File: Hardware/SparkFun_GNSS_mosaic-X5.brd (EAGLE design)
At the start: 63.5 x 50.8 mm, 169 parts, among them J3 MICROSD, J5 USB Female Type C Connector, U1 MOSAIC-X5X5, U2 SN74AHC1G125DBVR, U5 AP2112K-3.3V

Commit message: Route board.
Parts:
- removed U$1: (no value), output:MOSAIC_0
- removed U$139: (no value), output:MOSAIC0
- added R1: 10k, SparkFun-Resistors:0603
- added U$19: (no value), output:MOSAIC#X50
- added U$20: (no value), output:MOSAIC#X5_0
- moved U$87 2.54 mm to (15.2, 4.19)
- moved U$89 2.54 mm to (12.7, 4.06)
- moved U$93 2.54 mm to (15.2, 4.06)
- moved U$95 2.54 mm to (12.7, 3.94)
- moved C5 2.54 mm to (17.8, 27.9), turned to 0 degrees
- moved U$110 2.54 mm to (20.3, 46.7)
- moved U$113 2.54 mm to (17.8, 46.9)
- moved U$114 2.54 mm to (20.3, 46.6)
- moved U$117 2.54 mm to (17.8, 46.7)
- moved U$123 2.54 mm to (22.9, 47.0)
- moved U$124 2.54 mm to (25.4, 46.4)
- moved U$130 2.54 mm to (22.9, 47.0)
- moved U$131 2.54 mm to (25.4, 46.2)
- moved R17 1.27 mm to (10.2, 14.0)
- moved R16 1.27 mm to (10.2, 6.35)
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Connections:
- net PPS_18V renamed PPS_1V8
- new net N$5: J3.2, R1.1
- net 3.3V: now also R1.2
- net D+: now also D1.6; no longer D1.4
- net D-: now also D1.4; no longer D1.6
- net VIN: now also J7.3; no longer J7.4
- net V_USB: now also J7.4; no longer J7.3
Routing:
- net 3.3V: track 0.00 -> 155.8 mm, vias 0 -> 4
- net V_USB: track 0.00 -> 89.0 mm, vias 0 -> 4
- net LOG_BTN: track 0.00 -> 88.9 mm, vias 0 -> 4
- net SD_CMD: track 0.00 -> 70.2 mm, vias 0 -> 2
- net SD_CLK: track 0.00 -> 67.8 mm, vias 0 -> 2
- net SD_DATA: track 0.00 -> 67.2 mm, vias 0 -> 2
- net V_BAT: track 0.00 -> 66.3 mm, vias 0 -> 2
- net 5V: track 0.00 -> 66.0 mm, vias 0 -> 2
- net PPS_3V3: track 0.00 -> 59.0 mm, vias 0 -> 2
- net !RESET!: track 0.00 -> 51.6 mm, vias 0 -> 4
- net LOG_LED: track 0.00 -> 50.3 mm, vias 0 -> 3
- net COM3_CTS: track 0.00 -> 48.1 mm, vias 0 -> 2
- net VIN: track 0.00 -> 47.6 mm, vias 0 -> 1
- net COM3_TX: track 0.00 -> 47.1 mm, vias 0 -> 3
- net COM3_RX: track 0.00 -> 44.8 mm, vias 0 -> 2
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
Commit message: Add jumper to ant voltage. Add production panel.
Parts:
- removed C1: 0.1uF, SparkFun-Capacitors:0603
- removed J10: (no value), SparkFun-Connectors:1X06_NO_SILK
- removed L1: 39nH, SparkFun-Coils:0603
- removed U$78: (no value), output:GP1
- added ANT_V: (no value), SparkFun-Jumpers:SMT-JUMPER_3_1-NC_TRACE_SILK
- added D2: WHITE, SparkFun-LED:LED-0603
- added GP2: JUMPER-SMT_2_NC_TRACE_SILK, SparkFun-Jumpers:SMT-JUMPER_2_NC_TRACE_SILK
- added J6: (no value), SparkFun-Connectors:1X07_NO_SILK
- added Q9: 20V/0.2A/8MHz/1.2Ω/1Vth, SparkFun-DiscreteSemi:SOT-416FL
- added R46, R47: 2.2k, SparkFun-Resistors:0603
- added R6, R7: 169K, SparkFun-Resistors:0603@1
- added R9: 1k, SparkFun-Resistors:0603@1
- added U$1: (no value), output:V0
- added U$22: (no value), output:G1
- added U$23: (no value), output:3V30
- added U$24: (no value), output:5V0
- added U$26: (no value), output:#ANT_V#0
- added U$27: (no value), output:#RTK_LED#0
- added U$28: (no value), output:RTK0
- added U$29: (no value), output:PVT0
- R1, R10, R16, R17, R2, R3, R5, R8: device SparkFun-Resistors:0603 -> SparkFun-Resistors:0603@1
- R11, R4: value 1k -> 2.2k
- R12: value 1k -> 330; device SparkFun-Resistors:0603 -> SparkFun-Resistors:0603@1
- U$17: device output:#1 -> output:#_RTK#0
- U$7: device output:#0 -> output:#RTK#0
- U1: device Septentrio_Mosaic:MOSAIC-X5 -> Septentriom_mosaic-X5:MOSAIC_LGA
- moved U$7 47.0 mm to (45.7, 3.94), flipped to the top, turned to 90 degrees
- moved U$17 43.7 mm to (45.7, 4.06), turned to 270 degrees
- moved U$3 3.81 mm to (31.4, 21.6)
- moved U$4 3.81 mm to (31.2, 25.4)
- moved J1 2.54 mm to (25.4, 1.27)
- moved U$101 2.54 mm to (30.5, 3.94)
- moved U$102 2.54 mm to (25.4, 3.56)
- moved U$105 2.54 mm to (30.5, 3.68)
- moved U$106 2.54 mm to (25.4, 3.17)
- moved U$109 2.54 mm to (18.9, 7.62)
- moved J9 2.54 mm to (15.2, 1.27)
- moved U$87 2.54 mm to (12.7, 4.19)
- moved U$91 2.54 mm to (15.2, 3.56)
- moved U$93 2.54 mm to (12.7, 4.06)
- moved U$97 2.54 mm to (15.2, 3.17)
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- renumbered GP to GP1
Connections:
- net GP_LED renamed PVT_LED
- removed net ANT_VCC: C1.1, L1.2
- new net ANT_V: ANT_V.2, C3.1, FB1.1
- new net ICM-20948-LV_#_1.8V: Q9.1, R46.2
- new net N$6: R6.1, U1.AC6
- new net N$7: R7.1, U1.AC7
- new net N$8: D2.A, R9.1
- new net N$9: GP2.1, R9.2
- new net PPS_3: Q9.3, R47.1, U2.2
- new net RTK_LED: GP2.2, J6.3, U1.M3
- net 3.3V: now also ANT_V.1, R47.2
- net 5V: now also ANT_V.3; no longer C3.1, FB1.1
- net EVENTA: now also J6.6, R6.2; no longer J10.5, U1.AC6
- net EVENTB: now also J6.7, R7.2; no longer J10.6, U1.AC7
- net GND: now also D2.C, U1.V23; no longer C1.2
- net GP1: now also J6.1; no longer J10.1
- net GP2: now also J6.2; no longer J10.2
- net GPS_ANT1: no longer L1.1
- net LOG_BTN: now also J6.4; no longer J10.3
- net PPS_1V8: now also Q9.2, R46.1; no longer U2.2
- net PPS_3V3: now also J6.5; no longer J10.4
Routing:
- net RTK_LED: track 0.00 -> 51.6 mm, vias 0 -> 2
- net ANT_V: track 0.00 -> 17.1 mm, vias 0 -> 1
- net 5V: track 66.0 -> 49.0 mm, vias 2 -> 3
- net PPS_3: track 0.00 -> 15.6 mm
- net V_BAT: track 66.3 -> 52.3 mm, vias 2 -> 3
- net 3.3V: track 155.8 -> 165.9 mm, vias 4 -> 6
- net PPS_1V8: track 6.96 -> 15.9 mm
- net N$7: track 0.00 -> 4.91 mm
- net N$6: track 0.00 -> 4.65 mm
- net EVENTA: track 17.6 -> 22.1 mm
- net N$9: track 0.00 -> 4.06 mm, vias 0 -> 1
- net EVENTB: track 19.9 -> 23.4 mm
- net COM2_TX: track 10.7 -> 13.2 mm
- net ANT_VCC: track 2.32 -> 0.00 mm
- net GP1: track 31.0 -> 33.1 mm, vias 2 -> 1
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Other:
- board text added: "15"
- board text added: "2"
- board text added: "Material: TG155"

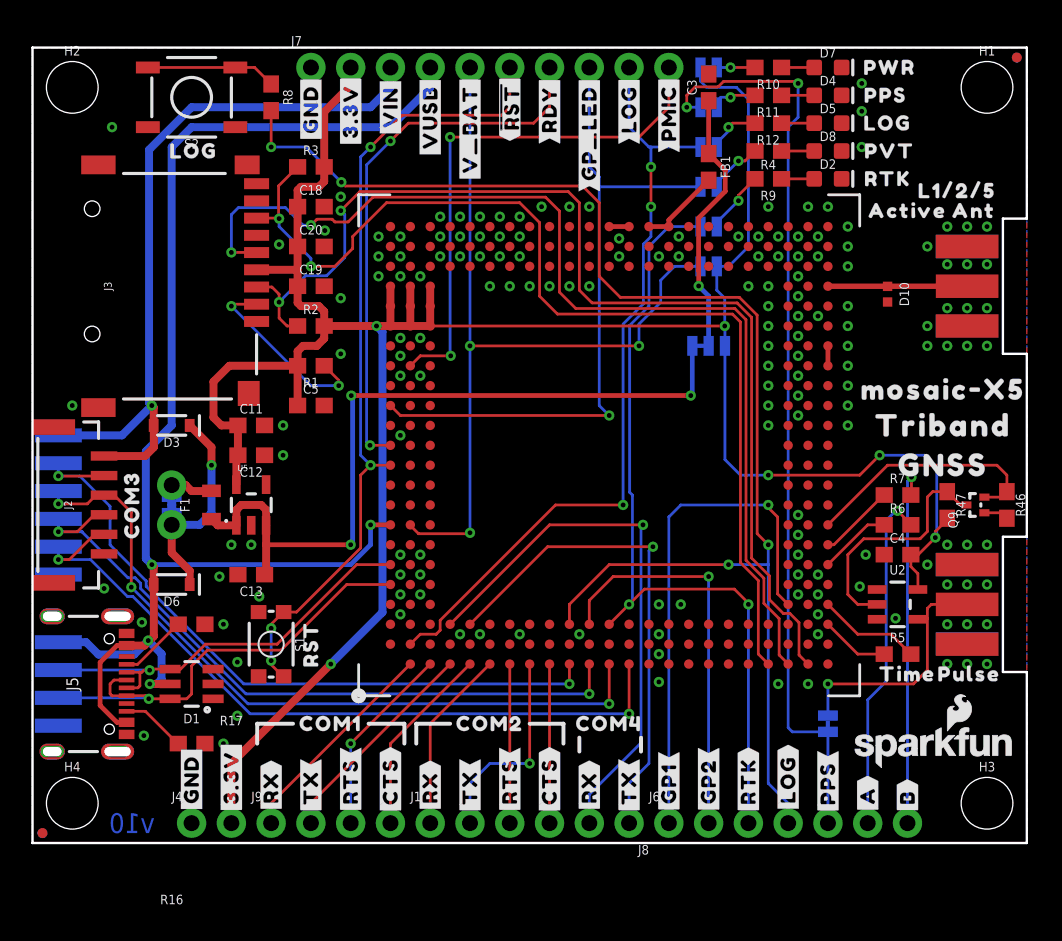
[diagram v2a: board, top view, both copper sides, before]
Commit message: Fixed tCream on mosaic pin 1.
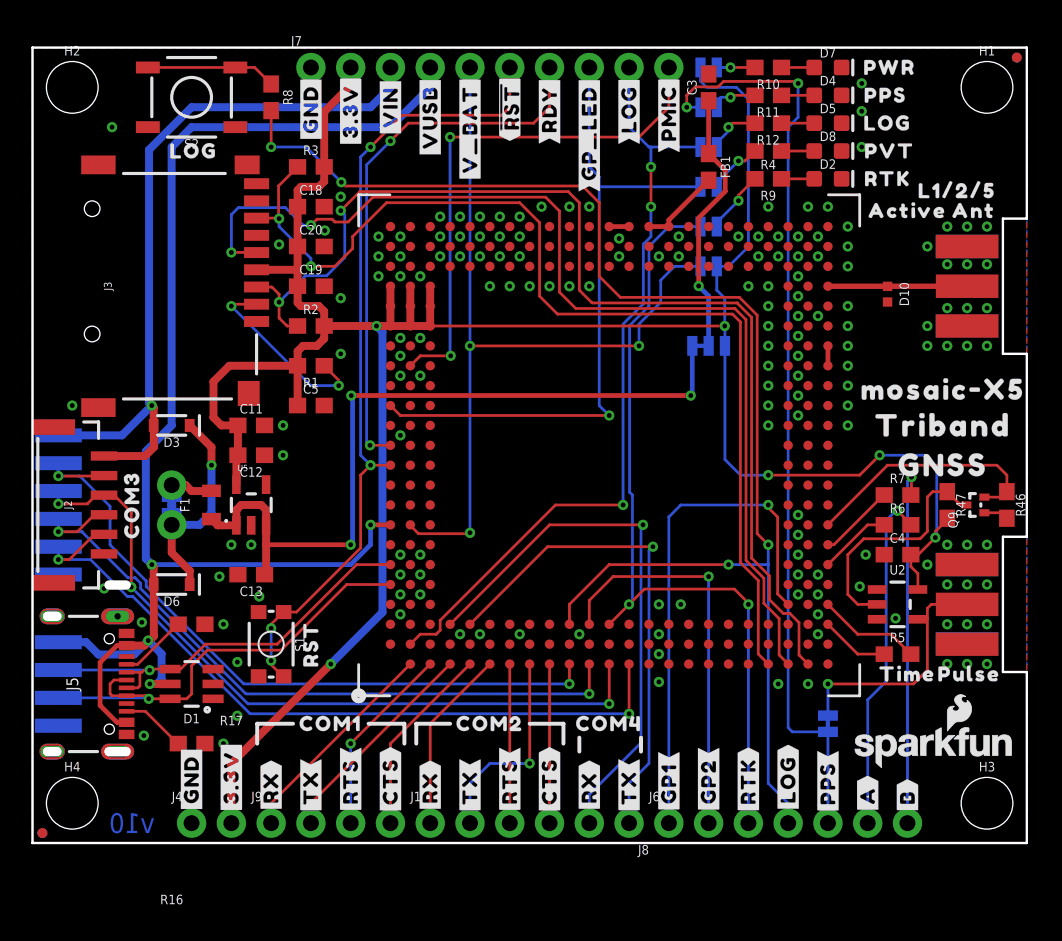
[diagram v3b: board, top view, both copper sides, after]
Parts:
- added U$30: (no value), output:MADE_IN_AMERICA0
- R1, R10, R12, R16, R17, R2, R3, R5, R6, R7, R8, R9: device SparkFun-Resistors:0603@1 -> SparkFun-Resistors:0603
- U1: device Septentriom_mosaic-X5:MOSAIC_LGA -> Septentrio_mosaic-X5:MOSAIC_LGA
- U5: value AP2112K-3.3V -> 3.3V
- moved LOGO1 3.81 mm to (31.8, 36.4)

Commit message: Add ESD and USB choke.
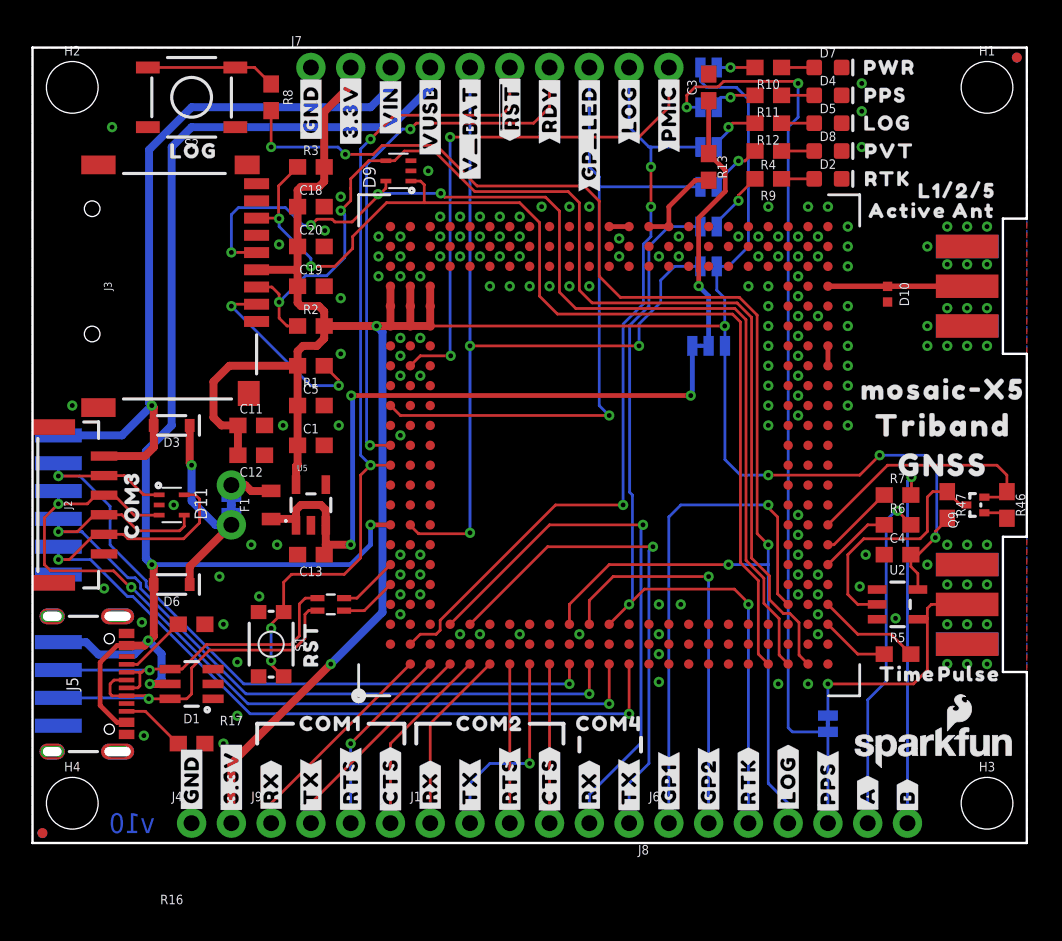
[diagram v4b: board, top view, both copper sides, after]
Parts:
- removed FB1: 470Ω, SparkFun-Coils:0603
- added C1: 10uF, SparkFun-Capacitors:0603
- added D11, D9: PESDXL4UGUG, SparkFun-DiscreteSemi:SOT353
- added R13: 0, SparkFun-Resistors:0603
- added T1: RFCMF1220100M4T, SparkFun-Coils:RFCMF1220100M4T
- moved C13 4.02 mm to (17.8, 18.4)
- moved F1 3.81 mm to (15.2, 21.6)
- moved U$5 3.81 mm to (14.6, 21.6)
- moved U5 3.81 mm to (17.8, 21.6)
- moved MEAS 3.81 mm to (12.7, 21.6)
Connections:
- new net USB_D+: D1.6, J5.A6, J5.B6, JP1.D+, T1.B1
- new net USB_D-: D1.4, J5.A7, J5.B7, JP1.D-, T1.A1
- net 3.3V: now also C1.1
- net ANT_V: now also R13.1; no longer FB1.1
- net COM3_CTS: now also D11.5
- net COM3_RTS: now also D11.4
- net COM3_RX: now also D11.1
- net COM3_TX: now also D11.3
- net D+: now also T1.B2; no longer D1.6, J5.A6, J5.B6, JP1.D+
- net D-: now also T1.A2; no longer D1.4, J5.A7, J5.B7, JP1.D-
- net GND: now also C1.2, D11.2, D9.2
- net SD_CLK: now also D9.5
- net SD_CMD: now also D9.4
- net SD_DATA: now also D9.1
- net VANT: now also R13.2; no longer FB1.2
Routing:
- net D+: track 29.7 -> 3.65 mm, vias 1 -> 0
- net USB_D+: track 0.00 -> 25.2 mm, vias 0 -> 1
- net D-: track 27.3 -> 3.85 mm, vias 1 -> 0
- net USB_D-: track 0.00 -> 23.0 mm, vias 0 -> 1
- net COM3_CTS: track 48.1 -> 57.4 mm
- net COM3_TX: track 47.1 -> 54.6 mm
- net COM3_RTS: track 44.5 -> 50.9 mm
- net 5V: track 49.0 -> 43.8 mm
- net COM3_RX: track 44.8 -> 48.8 mm
- net 3.3V: track 165.9 -> 169.1 mm
- net SD_CMD: track 70.2 -> 73.2 mm
- net SD_DATA: track 67.2 -> 69.3 mm
- net !RESET!: track 51.6 -> 53.4 mm
- net SD_CLK: track 67.8 -> 69.3 mm, vias 2 -> 4
- net LOG_BTN: track 88.9 -> 89.4 mm
